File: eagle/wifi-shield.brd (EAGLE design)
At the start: 101.6 x 53.3 mm, 15 parts, among them U1 USB-A-FEMALE

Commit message: added Arietta expansion connector
- to schematic, but not routed yet
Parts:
- removed JP15: POWER, SmartPrj:1X08
- removed U1: USB-A-FEMALE, te-conn-usb:USB-A-FEMALE
- added J1: USB, te-conn-usb:USB-A-FEMALE-RIGHT-ANGLE
- added JP10: Arietta Expansion Connector, adafruit:2X20
- added JP9: Arietta Connector, adafruit:2X20
- JP1: value Arietta Connector -> PWMH; device adafruit:2X20 -> SmartPrj:1X10
- JP7: value PWMH -> POWER; device SmartPrj:1X10 -> SmartPrj:1X08
- moved U$8 61.0 mm to (10.4, 17.4)
- moved JP7 48.7 mm to (36.8, 2.54)
- moved U$1 43.2 mm to (16.9, 27.4)
- moved JP1 32.5 mm to (30.2, 50.8)
- renumbered SPI to JP8
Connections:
- net D41 renamed N$41
- net D42 renamed N$42
- net D44 renamed N$44A
- removed net N$3 (its old number): JP15.1
- removed net N$571 (its old number): JP15.4
- removed net N$69 (its old number): JP15.8
- removed net N$71 (its old number): JP15.6
- removed net N$72 (its old number): JP15.3
- new net D1: JP10.1
- new net D10: JP10.10, JP9.10
- new net D11: JP10.11, JP9.11
- new net D12: JP10.12, JP9.12
- new net D13: JP10.13, JP9.13
- new net D14: JP10.14, JP9.14
- new net D15: JP10.15, JP9.15
- new net D16: JP10.16, JP9.16
- new net D17: JP10.17, JP9.17
- new net D18: JP10.18, JP9.18
- new net D19: JP10.19, JP9.19
- new net D2: JP10.2, JP9.2
- new net D20: JP10.20, JP9.20
- new net D21: JP10.21, JP9.21
- new net D22: JP10.22, JP9.22
- new net D23: JP10.23, JP9.23
- new net D24: JP10.24, JP9.24
- new net D25: JP10.25, JP9.25
- new net D26: JP10.26, JP9.26
- new net D27: JP10.27, JP9.27
- new net D28: JP10.28, JP9.28
- new net D29: JP10.29, JP9.29
- new net D3: JP10.3, JP9.3
- new net D30: JP10.30, JP9.30
- new net D31: JP10.31, JP9.31
- new net D32: JP10.32, JP9.32
- new net D33: JP10.33, JP9.33
- new net D34: JP10.34, JP9.34
- new net D35: JP10.35, JP9.35
- new net D36: JP10.36, JP9.36
- new net D37: JP10.37, JP9.37
- new net D5: JP10.5, JP9.5
- new net D7: JP10.7, JP9.7
- new net D8: JP10.8, JP9.8
- new net D9: JP10.9
- new net N$10: JP1.6
- new net N$38: JP4.19
- new net N$39: JP4.20
- new net N$40: JP4.21
- new net N$574: JP1.1
- new net N$576: JP1.8
- new net N$7: JP1.3
- new net N$8: JP1.4
- net 5V: now also J1.5V, JP9.1; no longer JP1.1, U1.5V
- net D38: now also JP10.38, JP9.38; no longer JP4.19
- net D39: now also JP10.39, JP9.39; no longer JP4.20
- net D40: now also JP10.40, JP9.40; no longer JP4.21
- net D_N: now also J1.D_N, JP10.4, JP9.4; no longer JP1.4, U1.D_N
- net D_P: now also J1.D_P, JP10.6, JP9.6; no longer JP1.6, U1.D_P
- net GND: now also J1.GND, JP7.7, JP9.9; no longer JP1.9, JP15.7, U1.GND
- net N$1: now also JP1.9; no longer JP7.9
- net N$11: now also JP1.7; no longer JP7.7
- net N$12: now also JP1.10; no longer JP7.10
- net N$575: now also JP1.2; no longer JP7.2
- net N$9: now also JP1.5; no longer JP7.5
- net VCC: now also JP7.2; no longer JP15.2
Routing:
- net D_P: track 53.2 -> 36.3 mm
- net D_N: track 51.3 -> 36.8 mm
- added copper zone on layer 1, net 5V
- added copper zone on layer 16, net GND
- removed copper zone on layer 16, net 5V
- removed copper zone on layer 1, net GND
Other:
- board text added: "StarCat Wifi Shield"
- board text removed: "StarCat Arietta Shield"

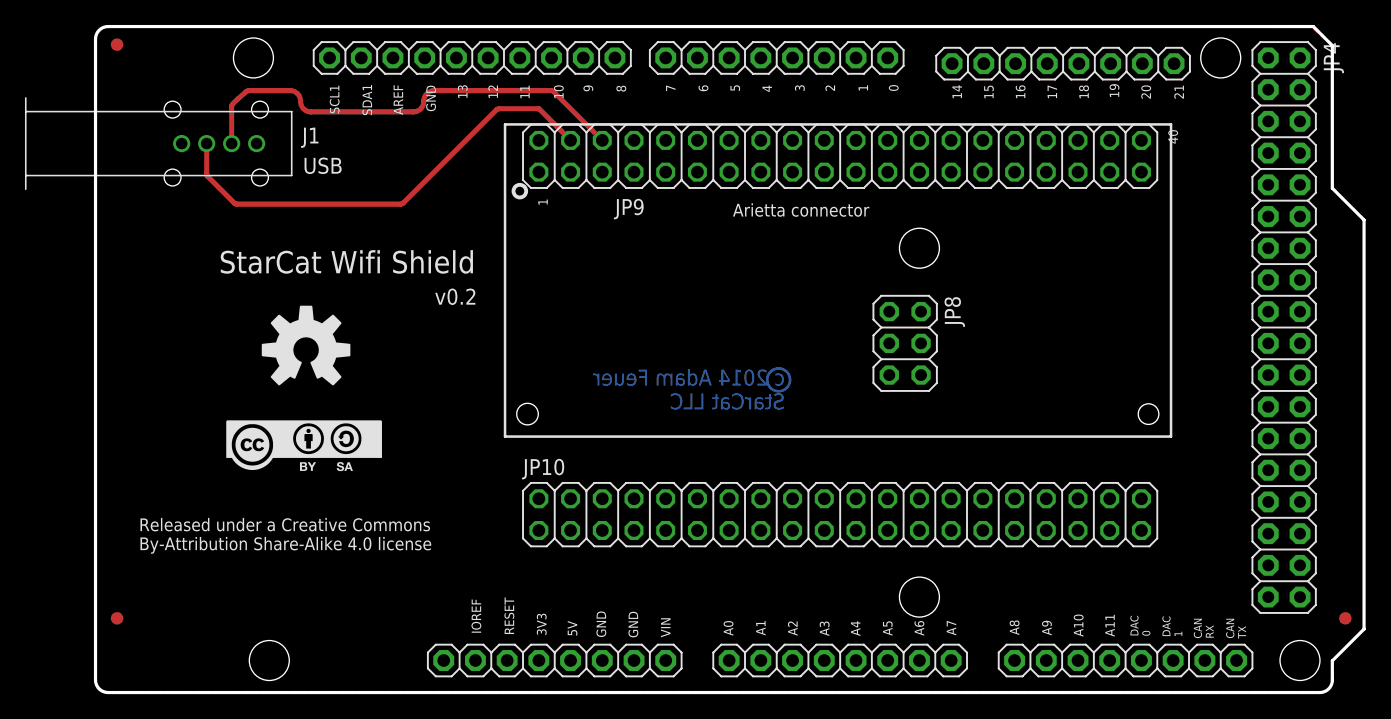
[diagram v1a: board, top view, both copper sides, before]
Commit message: corrected and routed Arietta auxiliary connector
- net classes are correct
- ERC and DRC pass
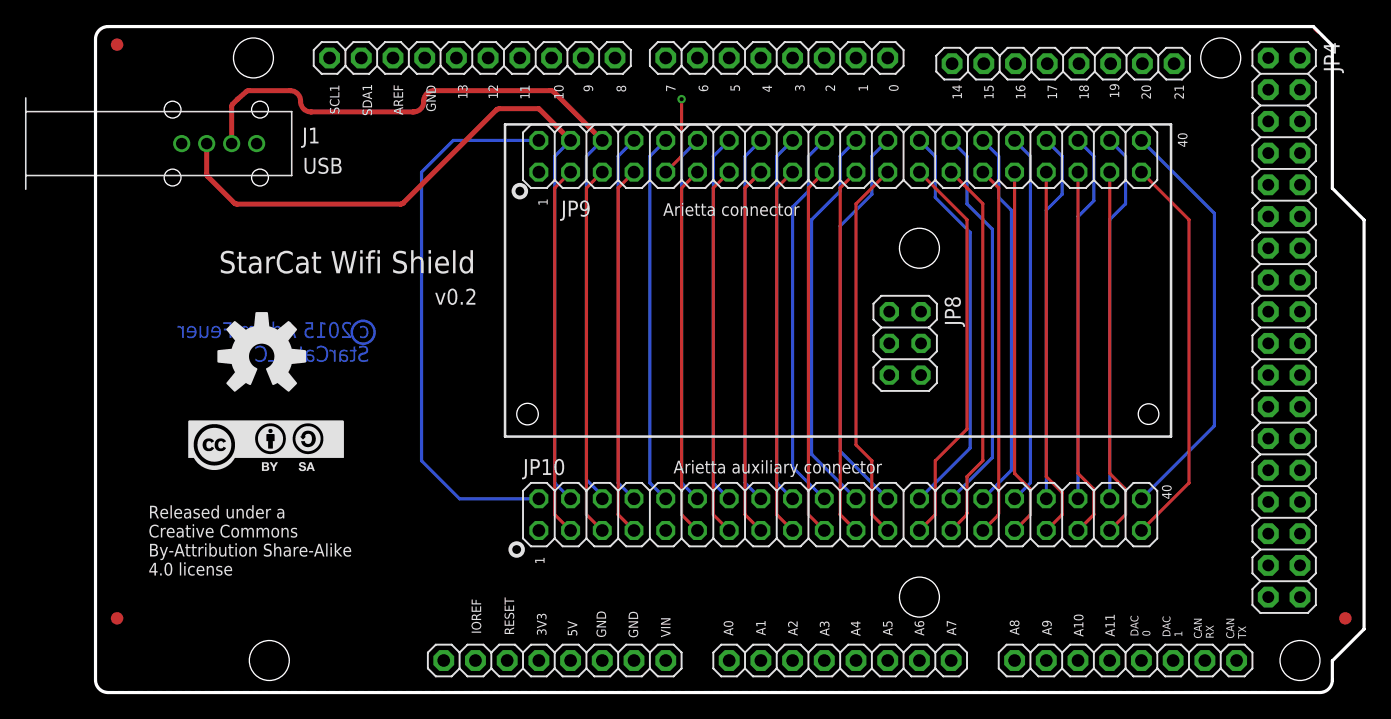
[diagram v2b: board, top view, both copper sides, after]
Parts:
- moved U$1 3.59 mm to (13.4, 26.9)
- moved U$8 3.05 mm to (7.37, 17.4)
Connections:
- removed net D1: JP10.1
- removed net D9: JP10.9
- new net GND1: JP8.6
- net 5V: now also JP10.1
- net GND: now also JP10.9; no longer JP8.6
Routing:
- net D2: track 0.00 -> 44.2 mm
- net D40: track 0.00 -> 33.5 mm
- net D26: track 0.00 -> 32.1 mm
- net D39: track 0.00 -> 31.9 mm
- net D24: track 0.00 -> 31.9 mm
- net D25: track 0.00 -> 31.9 mm
- net D22: track 0.00 -> 31.6 mm
- net D28: track 0.00 -> 31.4 mm
- net D20: track 0.00 -> 30.8 mm
- net D23: track 0.00 -> 30.8 mm
- net D27: track 0.00 -> 30.8 mm
- net D30: track 0.00 -> 30.6 mm
- net D36: track 0.00 -> 29.8 mm
- net D35: track 0.00 -> 29.8 mm
- net D32: track 0.00 -> 29.8 mm
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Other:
- board text added: "Arietta auxiliary connector"
- board text added: "c 2015 Adam Feuer StarCat LLC"
- board text removed: "c 2014 Adam Feuer StarCat LLC"
